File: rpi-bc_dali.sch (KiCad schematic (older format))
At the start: 5 parts, among them J1 Raspberry_Pi_2_3, J2 Conn_01x04, J3 Conn_01x04, J4 Conn_01x04, J5 Conn_01x04

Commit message: master : schematic update
 - first pass schematic.
 - annotated.
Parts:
- added D1, D2, D3, D4: LED, symbol Device:LED
- added D5: BZX84Cxx, Diode_SMD:D_SOT-23_ANK, symbol Diode:BZX84Cxx
- added D6: MB2S, Package_TO_SOT_SMD:TO-269AA, symbol Diode_Bridge:MB2S
- added Q1: BCX56, Package_TO_SOT_SMD:SOT-89-3, symbol Transistor_BJT:BCX56
- added R1, R8: 390R, symbol Device:R
- added R2, R3, R4, R5, R6: 1K, symbol Device:R
- added R7: 3K3, symbol Device:R
- added R9: 560R, symbol Device:R
- added U1, U2: HCPL-181, symbol Isolator:HCPL-181
- added U3: PSSI2021SAY, symbol Reference_Current:PSSI2021SAY
- renumbered J4 to J2, J5 to J4, J2 to J5
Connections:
- net at J5.1 (Pin_1): now also J5.2 (Pin_2), D6.2 (~~)
- net at J5.3 (Pin_3): now also J5.4 (Pin_4), D6.1 (~~)
- net CSN: now reaches J3.1 (Pin_1)
- net CSN: now also J1.24 (~CE0~/GPIO8)
- net MISO: now reaches J3.2 (Pin_2)
- net MISO: now also J1.21 (MISO0/GPIO9)
- net MOSI: now reaches J3.3 (Pin_3)
- net MOSI: now also J1.19 (MOSI0/GPIO10)
- net SCLK: now reaches J3.4 (Pin_4)
- net SCLK: now also J1.23 (SCLK0/GPIO11)
- net I2C_SDA: now reaches J2.1 (Pin_1)
- net I2C_SDA: now also J1.3 (SDA/GPIO2)
- net I2C_SCL: now reaches J2.2 (Pin_2)
- net I2C_SCL: now also J1.5 (SCL/GPIO3)
- net UART_TXD: now reaches J2.3 (Pin_3)
- net UART_TXD: now also J1.8 (GPIO14/TXD)
- net UART_RXD: now reaches J2.4 (Pin_4)
- net UART_RXD: now also J1.10 (GPIO15/RXD)
- net +5V: now reaches J4.1 (Pin_1)
- net +5V: now also J1.2 (5V), J1.4 (5V), J4.2 (Pin_2)
- net GND: now reaches J4.3 (Pin_3)
- net GND: now also J1.14 (GND), J1.20 (GND), J1.25 (GND), J1.30 (GND), J1.34 (GND), J1.39 (GND), J1.6 (GND), J1.9 (GND), J4.4 (Pin_4), U2.3 (Emitter)
- net +3V3: now reaches J1.1 (3V3)
- net +3V3: now also J1.17 (3V3), R2.1, R3.1, R4.1, R5.1, R7.1, U1.1 (Anode)
- net LED1: now reaches J1.11 (GPIO17)
- net LED1: now also D3.1 (K)
- net DALI_TX: now reaches J1.15 (GPIO22)
- net DALI_TX: now also R1.2
- net DALI_RX: now reaches J1.16 (GPIO23)
- net DALI_RX: now also R7.2, U2.4 (Collector)
- net LED3: now reaches J1.32 (PWM0/GPIO12)
- net LED3: now also D1.1 (K)
- net LED2: now reaches J1.33 (PWM1/GPIO13)
- net LED2: now also D2.1 (K)
- net LED0: now reaches J1.36 (GPIO16)
- net LED0: now also D4.1 (K)
- new net: R1.1, U1.2 (Cathode)
- new net: R6.1, R8.2, U1.3 (Emitter)
- new net: D5.1 (K), D6.3 (+), Q1.2 (C), U1.4 (Collector)
- new net: U2.1 (Anode), U3.2 (IOUT)
- new net: R9.2, U3.4 (REXT)
- new net: D5.2 (A), R9.1, U3.5 (VS)
- new net: Q1.1 (B), R8.1
- new net: D1.2 (A), R2.2
- new net: D2.2 (A), R3.2
- new net: D3.2 (A), R4.2
- new net: D4.2 (A), R5.2
- new net GND_ISO: D6.4 (-), Q1.3 (E), R6.2, U2.2 (Cathode), U3.3 (GND)
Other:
- moved on the sheet: J1, J2, J3, J4, J5

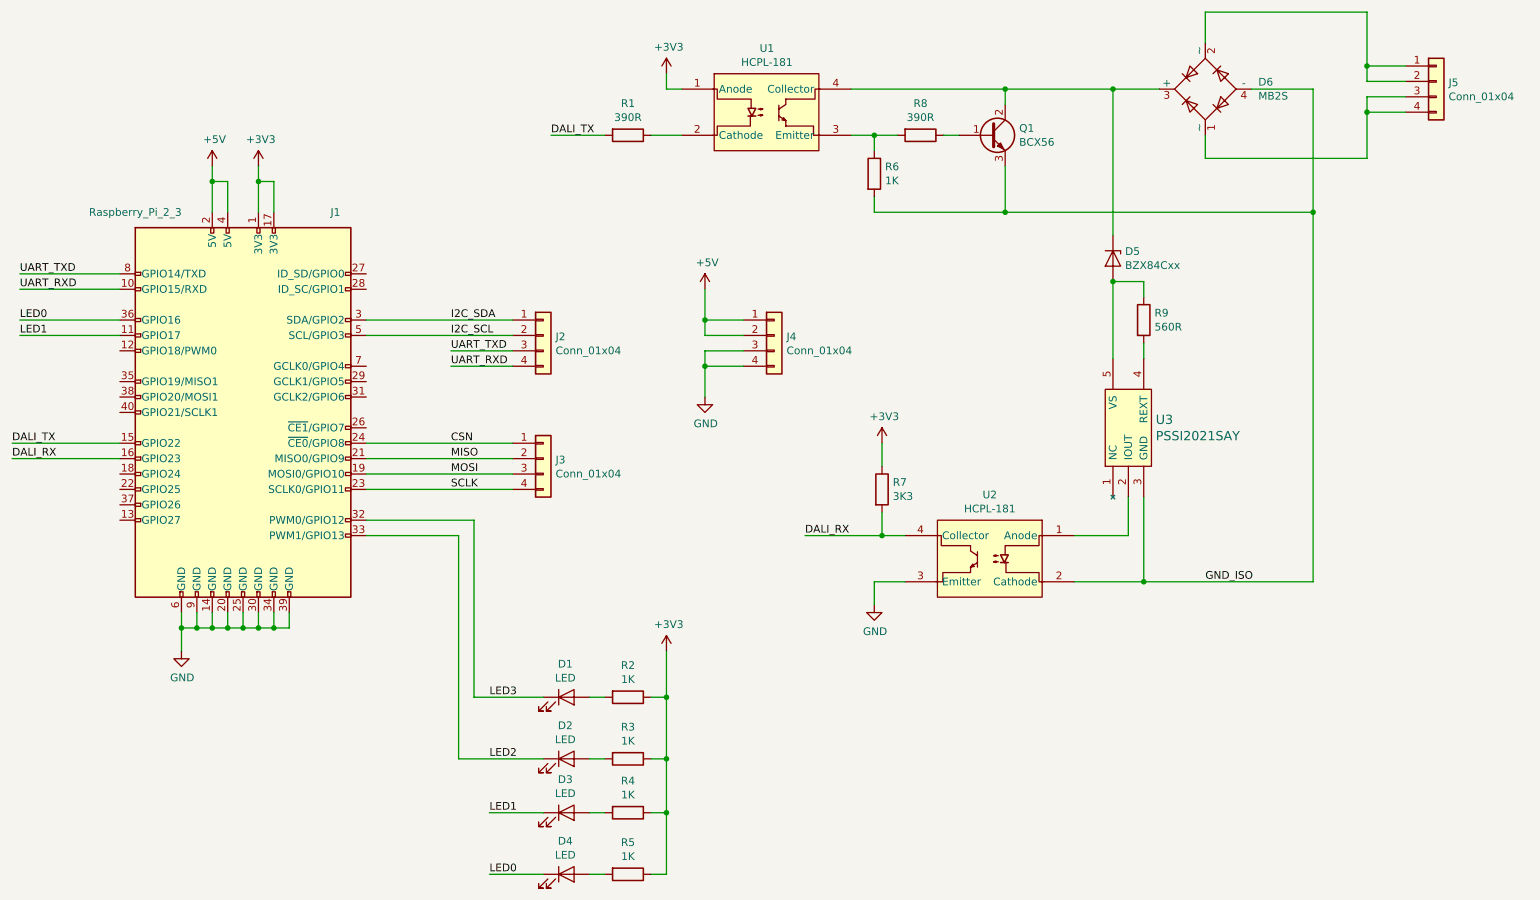
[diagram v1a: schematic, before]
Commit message: master : first pass at layout
 - minor adjustments to schematic for trace flow
 - all nets routed and polygon's poured.
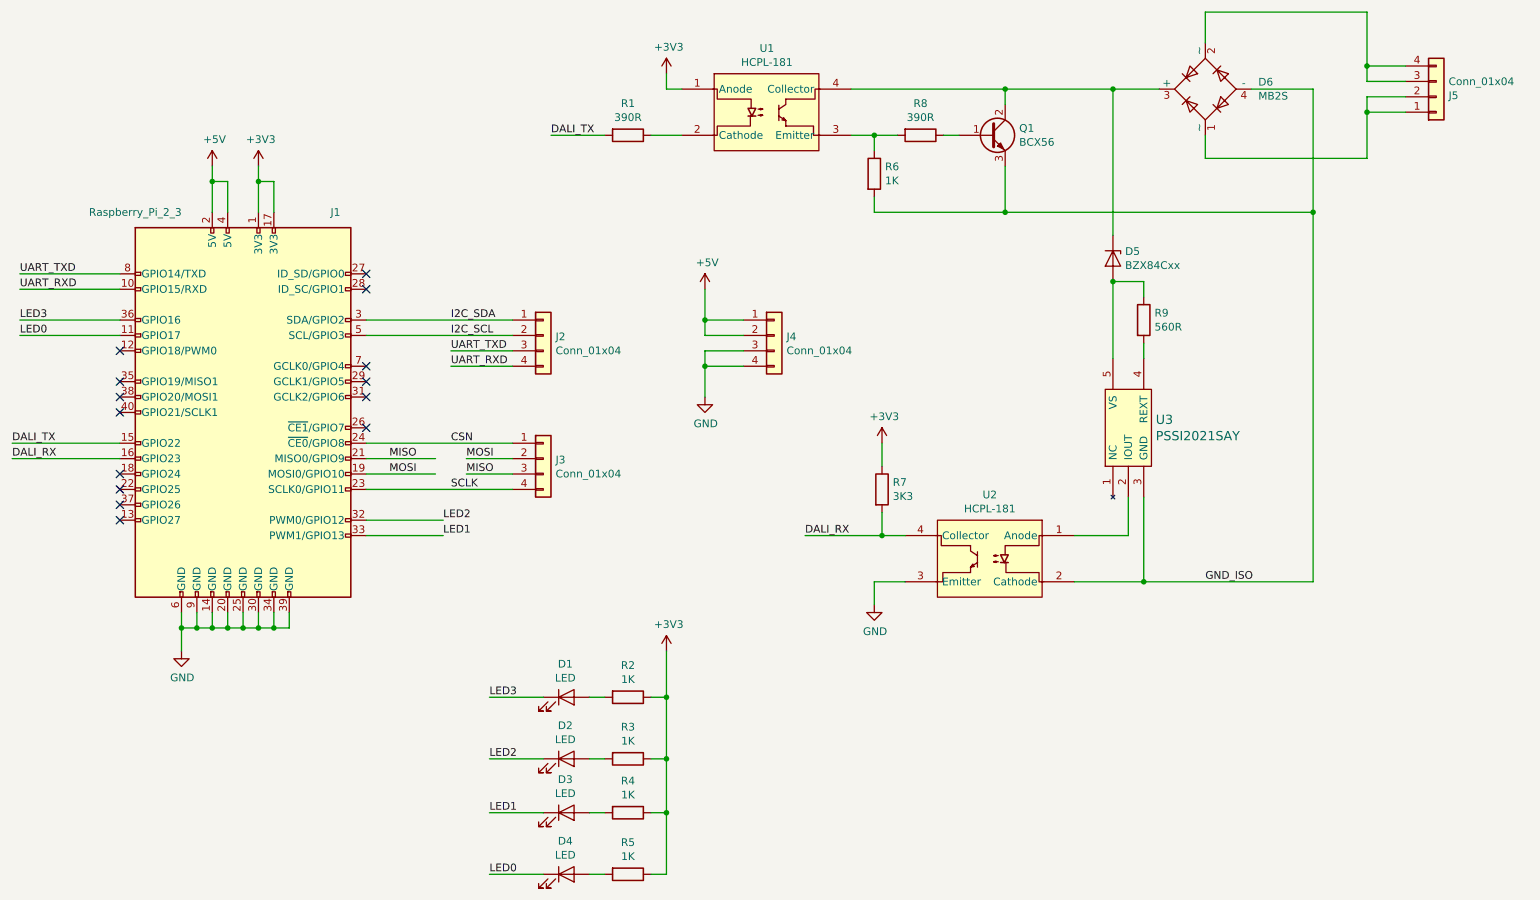
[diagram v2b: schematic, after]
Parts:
- D1, D2, D3, D4: footprint (none) -> LED_SMD:LED_0603_1608Metric_Pad1.05x0.95mm_HandSolder
- R1, R2, R3, R4, R5, R6, R7, R8, R9: footprint (none) -> Resistor_SMD:R_0603_1608Metric_Pad1.05x0.95mm_HandSolder
- U1, U2: footprint (none) -> Package_SO:SO-4_4.4x3.6mm_P2.54mm
- U3: footprint (none) -> Package_TO_SOT_SMD:SOT-353_SC-70-5_Handsoldering
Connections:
- net LED0: now also J1.11 (GPIO17); no longer J1.36 (GPIO16)
- net LED1: now also J1.33 (PWM1/GPIO13); no longer J1.11 (GPIO17)
- net LED2: now also J1.32 (PWM0/GPIO12); no longer J1.33 (PWM1/GPIO13)
- net LED3: now also J1.36 (GPIO16); no longer J1.32 (PWM0/GPIO12)
- net MISO: now also J3.3 (Pin_3); no longer J3.2 (Pin_2)
- net MOSI: now also J3.2 (Pin_2); no longer J3.3 (Pin_3)
- net at J5.1 (Pin_1), J5.2 (Pin_2): now also D6.1 (~~); no longer D6.2 (~~)
- net at J5.3 (Pin_3), J5.4 (Pin_4): now also D6.2 (~~); no longer D6.1 (~~)
- no-connect marks 0 -> 14
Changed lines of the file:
@@
 $EndDescr
-$Comp
-L Connector_Generic:Conn_01x04 J5
-U 1 1 5BC9039B
-P 10400 1500
-F 0 "J5" H 10480 1492 50  0000 L CNN
-F 1 "Conn_01x04" H 10480 1401 50  0000 L CNN
-F 2 "TerminalBlock_Phoenix:TerminalBlock_Phoenix_PTSM-0,5-4-HH-2,5-THR_1x04_P2.50mm_Horizontal" H 10400 1500 50  0001 C CNN
-F 3 "~" H 10400 1500 50  0001 C CNN
-	1    10400 1500
-	1    0    0    -1
-$EndComp
 $Comp
 L Connector_Generic:Conn_01x04 J3
@@
 F 0 "U3" V 8453 3572 60  0000 R CNN
 F 1 "PSSI2021SAY" V 8347 3572 60  0000 R CNN
-F 2 "" H 8400 3750 60  0001 C CNN
+F 2 "Package_TO_SOT_SMD:SOT-353_SC-70-5_Handsoldering" H 8400 3750 60  0001 C CNN
 F 3 "https://assets.nexperia.com/documents/data-sheet/PSSI2021SAY.pdf" H 8400 3750 60  0001 C CNN
 	1    8400 3750
@@
 F 0 "U2" H 7500 4915 50  0000 C CNN
 F 1 "HCPL-181" H 7500 4824 50  0000 C CNN
-F 2 "" H 7100 4800 50  0001 C CNN
+F 2 "Package_SO:SO-4_4.4x3.6mm_P2.54mm" H 7100 4800 50  0001 C CNN
 F 3 "" H 7100 4800 50  0001 C CNN
 	1    7500 4550
@@
 F 0 "U1" H 6052 2015 50  0000 C CNN
 F 1 "HCPL-181" H 6052 1924 50  0000 C CNN
-F 2 "" H 5650 1900 50  0001 C CNN
+F 2 "Package_SO:SO-4_4.4x3.6mm_P2.54mm" H 5650 1900 50  0001 C CNN
 F 3 "" H 5650 1900 50  0001 C CNN
 	1    6050 1650
@@
 F 0 "R9" H 8570 3096 50  0000 L CNN
 F 1 "560R" H 8570 3005 50  0000 L CNN
-F 2 "" V 8430 3050 50  0001 C CNN
+F 2 "Resistor_SMD:R_0603_1608Metric_Pad1.05x0.95mm_HandSolder" V 8430 3050 50  0001 C CNN
 F 3 "~" H 8500 3050 50  0001 C CNN
 	1    8500 3050
@@
 F 0 "R7" H 6870 4196 50  0000 L CNN
 F 1 "3K3" H 6870 4105 50  0000 L CNN
-F 2 "" V 6730 4150 50  0001 C CNN
+F 2 "Resistor_SMD:R_0603_1608Metric_Pad1.05x0.95mm_HandSolder" V 6730 4150 50  0001 C CNN
 F 3 "~" H 6800 4150 50  0001 C CNN
 	1    6800 4150
@@
 F 0 "R1" V 4943 1850 50  0000 C CNN
 F 1 "390R" V 5034 1850 50  0000 C CNN
-F 2 "" V 5080 1850 50  0001 C CNN
+F 2 "Resistor_SMD:R_0603_1608Metric_Pad1.05x0.95mm_HandSolder" V 5080 1850 50  0001 C CNN
 F 3 "~" H 5150 1850 50  0001 C CNN
 	1    5150 1850
@@
 F 0 "R6" H 6820 2146 50  0000 L CNN
 F 1 "1K" H 6820 2055 50  0000 L CNN
-F 2 "" V 6680 2100 50  0001 C CNN
+F 2 "Resistor_SMD:R_0603_1608Metric_Pad1.05x0.95mm_HandSolder" V 6680 2100 50  0001 C CNN
 F 3 "~" H 6750 2100 50  0001 C CNN
 	1    6750 2100
@@
 F 0 "R8" V 6843 1850 50  0000 C CNN
 F 1 "390R" V 6934 1850 50  0000 C CNN
-F 2 "" V 6980 1850 50  0001 C CNN
+F 2 "Resistor_SMD:R_0603_1608Metric_Pad1.05x0.95mm_HandSolder" V 6980 1850 50  0001 C CNN
 F 3 "~" H 7050 1850 50  0001 C CNN
 	1    7050 1850
@@
 	8900 2000 9950 2000
 Wire Wire Line
-	9950 2000 9950 1700
-Wire Wire Line
-	9950 1700 10200 1700
-Wire Wire Line
 	8900 1250 8900 1050
 Wire Wire Line
 	8900 1050 9950 1050
-Wire Wire Line
-	9950 1050 9950 1400
-Wire Wire Line
-	9950 1400 10200 1400
-Wire Wire Line
-	10200 1500 9950 1500
-Wire Wire Line
-	9950 1500 9950 1400
-Connection ~ 9950 1400
-Wire Wire Line
-	10200 1600 9950 1600
-Wire Wire Line
-	9950 1600 9950 1700
-Connection ~ 9950 1700
 Wire Wire Line
 	7600 1550 8300 1550
@@
 	3450 3850 4400 3850
 Wire Wire Line
-	3450 3950 4400 3950
-Wire Wire Line
-	3450 4050 4400 4050
+	3450 3950 3900 3950
+Wire Wire Line
+	3450 4050 3900 4050
 Wire Wire Line
 	3450 4150 4400 4150
@@
 Text Label 4000 3850 0    50   ~ 0
 CSN
-Text Label 4000 3950 0    50   ~ 0
+Text Label 3600 3950 0    50   ~ 0
 MISO
-Text Label 4000 4050 0    50   ~ 0
+Text Label 3600 4050 0    50   ~ 0
 MOSI
 Text Label 4000 4150 0    50   ~ 0
@@
 F 0 "D1" H 4743 5716 50  0000 C CNN
 F 1 "LED" H 4743 5625 50  0000 C CNN
-F 2 "" H 4750 5500 50  0001 C CNN
+F 2 "LED_SMD:LED_0603_1608Metric_Pad1.05x0.95mm_HandSolder" H 4750 5500 50  0001 C CNN
 F 3 "~" H 4750 5500 50  0001 C CNN
 	1    4750 5500
@@
 F 0 "D2" H 4743 6116 50  0000 C CNN
 F 1 "LED" H 4743 6025 50  0000 C CNN
-F 2 "" H 4750 5900 50  0001 C CNN
+F 2 "LED_SMD:LED_0603_1608Metric_Pad1.05x0.95mm_HandSolder" H 4750 5900 50  0001 C CNN
 F 3 "~" H 4750 5900 50  0001 C CNN
 	1    4750 5900
@@
 F 0 "D3" H 4743 6466 50  0000 C CNN
 F 1 "LED" H 4743 6375 50  0000 C CNN
-F 2 "" H 4750 6250 50  0001 C CNN
+F 2 "LED_SMD:LED_0603_1608Metric_Pad1.05x0.95mm_HandSolder" H 4750 6250 50  0001 C CNN
 F 3 "~" H 4750 6250 50  0001 C CNN
 	1    4750 6250
@@
 F 0 "D4" H 4743 6866 50  0000 C CNN
 F 1 "LED" H 4743 6775 50  0000 C CNN
-F 2 "" H 4750 6650 50  0001 C CNN
+F 2 "LED_SMD:LED_0603_1608Metric_Pad1.05x0.95mm_HandSolder" H 4750 6650 50  0001 C CNN
 F 3 "~" H 4750 6650 50  0001 C CNN
 	1    4750 6650
@@
 F 0 "R2" V 4943 5500 50  0000 C CNN
 F 1 "1K" V 5034 5500 50  0000 C CNN
-F 2 "" V 5080 5500 50  0001 C CNN
+F 2 "Resistor_SMD:R_0603_1608Metric_Pad1.05x0.95mm_HandSolder" V 5080 5500 50  0001 C CNN
 F 3 "~" H 5150 5500 50  0001 C CNN
 	1    5150 5500
@@
 F 0 "R3" V 4943 5900 50  0000 C CNN
 F 1 "1K" V 5034 5900 50  0000 C CNN
-F 2 "" V 5080 5900 50  0001 C CNN
+F 2 "Resistor_SMD:R_0603_1608Metric_Pad1.05x0.95mm_HandSolder" V 5080 5900 50  0001 C CNN
 F 3 "~" H 5150 5900 50  0001 C CNN
 	1    5150 5900
@@
 F 0 "R4" V 4943 6250 50  0000 C CNN
 F 1 "1K" V 5034 6250 50  0000 C CNN
-F 2 "" V 5080 6250 50  0001 C CNN
+F 2 "Resistor_SMD:R_0603_1608Metric_Pad1.05x0.95mm_HandSolder" V 5080 6250 50  0001 C CNN
 F 3 "~" H 5150 6250 50  0001 C CNN
 	1    5150 6250
@@
 F 0 "R5" V 4943 6650 50  0000 C CNN
 F 1 "1K" V 5034 6650 50  0000 C CNN
-F 2 "" V 5080 6650 50  0001 C CNN
+F 2 "Resistor_SMD:R_0603_1608Metric_Pad1.05x0.95mm_HandSolder" V 5080 6650 50  0001 C CNN
 F 3 "~" H 5150 6650 50  0001 C CNN
 	1    5150 6650
@@
 	4900 6650 5000 6650
 Wire Wire Line
-	4600 5500 4150 5500
-Wire Wire Line
-	4150 5500 4150 4350
-Wire Wire Line
-	4150 4350 3450 4350
-Wire Wire Line
-	3450 4450 4050 4450
-Wire Wire Line
-	4050 4450 4050 5900
-Wire Wire Line
-	4050 5900 4600 5900
+	4600 5500 4250 5500
+Wire Wire Line
+	3950 4350 3450 4350
+Wire Wire Line
+	3450 4450 3950 4450
+Wire Wire Line
+	4250 5900 4600 5900
 Wire Wire Line
 	1850 3050 1200 3050
@@
 Text Label 4250 5500 0    50   ~ 0
 LED3
+Text Label 1200 3150 0    50   ~ 0
+LED0
+NoConn ~ 3450 2750
+NoConn ~ 3450 2850
+NoConn ~ 3450 3350
+NoConn ~ 3450 3450
+NoConn ~ 3450 3550
+NoConn ~ 3450 3750
+NoConn ~ 1850 4350
+NoConn ~ 1850 4250
+NoConn ~ 1850 4150
+NoConn ~ 1850 4050
+NoConn ~ 1850 3650
+NoConn ~ 1850 3550
+NoConn ~ 1850 3450
+NoConn ~ 1850 3250
+$Comp
+L Connector_Generic:Conn_01x04 J5
+U 1 1 5BC9039B
+P 10400 1600
+F 0 "J5" H 10480 1592 50  0000 L CNN
+F 1 "Conn_01x04" H 10480 1501 50  0000 L CNN
+F 2 "TerminalBlock_Phoenix:TerminalBlock_Phoenix_PTSM-0,5-4-HH-2,5-THR_1x04_P2.50mm_Horizontal" H 10400 1600 50  0001 C CNN
+F 3 "~" H 10400 1600 50  0001 C CNN
+	1    10400 1600
+	1    0    0    1
+$EndComp
+Wire Wire Line
+	9950 1500 9950 1400
+Wire Wire Line
+	9950 1050 9950 1400
+Connection ~ 9950 1400
+Wire Wire Line
+	9950 1400 10200 1400
+Wire Wire Line
+	10200 1500 9950 1500
+Wire Wire Line
+	9950 1600 9950 1700
+Wire Wire Line
+	9950 2000 9950 1700
+Connection ~ 9950 1700
+Wire Wire Line
+	9950 1700 10200 1700
+Wire Wire Line
+	10200 1600 9950 1600
+Text Label 3950 4450 0    50   ~ 0
+LED1
+Text Label 3950 4350 0    50   ~ 0
+LED2
 Text Label 1200 3050 0    50   ~ 0
-LED0
-Text Label 1200 3150 0    50   ~ 0
-LED1
+LED3
+Wire Wire Line
+	4400 3950 4100 3950
+Wire Wire Line
+	4400 4050 4100 4050
+Text Label 4100 3950 0    50   ~ 0
+MOSI
+Text Label 4100 4050 0    50   ~ 0
+MISO
 $EndSCHEMATC

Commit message: master: updates to layout
 - fixed placement bug in GPIO connector.
 - re-routed all nets.
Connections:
- net LED0: now also J1.35 (GPIO19/MISO1); no longer J1.11 (GPIO17)
- net LED3: now also J1.31 (GCLK2/GPIO6); no longer J1.36 (GPIO16)
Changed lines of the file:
@@
 EESchema Schematic File Version 4
-LIBS:rpi-bc_dali-cache
 EELAYER 30 0
 EELAYER END
@@
 	4250 5900 4600 5900
 Wire Wire Line
-	1850 3050 1200 3050
-Wire Wire Line
-	1850 3150 1200 3150
+	4100 3550 3450 3550
 Wire Wire Line
 	4600 6250 4250 6250
@@
 Text Label 4250 5500 0    50   ~ 0
 LED3
-Text Label 1200 3150 0    50   ~ 0
-LED0
 NoConn ~ 3450 2750
 NoConn ~ 3450 2850
 NoConn ~ 3450 3350
 NoConn ~ 3450 3450
-NoConn ~ 3450 3550
 NoConn ~ 3450 3750
 NoConn ~ 1850 4350
@@
 NoConn ~ 1850 3650
 NoConn ~ 1850 3550
-NoConn ~ 1850 3450
 NoConn ~ 1850 3250
 $Comp
@@
 Text Label 3950 4350 0    50   ~ 0
 LED2
-Text Label 1200 3050 0    50   ~ 0
+Text Label 4100 3550 0    50   ~ 0
 LED3
 Wire Wire Line
@@
 Text Label 4100 4050 0    50   ~ 0
 MISO
+Wire Wire Line
+	1850 3450 1200 3450
+Text Label 1200 3450 0    50   ~ 0
+LED0
+NoConn ~ 1850 3050
+NoConn ~ 1850 3150
 $EndSCHEMATC
